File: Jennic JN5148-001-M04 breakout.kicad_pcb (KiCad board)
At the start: 2 copper layers, 45.7 x 55.9 mm, 23 parts, among them J1 Conn_01x21_Male, J2 Conn_01x21_Male, J9 Conn_01x06_Male, SW1 SW_Push, SW2 SW_Push, SW5 SW_Push, SW7 SW_Push, U1 JN5148-001-M04, U2 NCP1117LPST33T3G

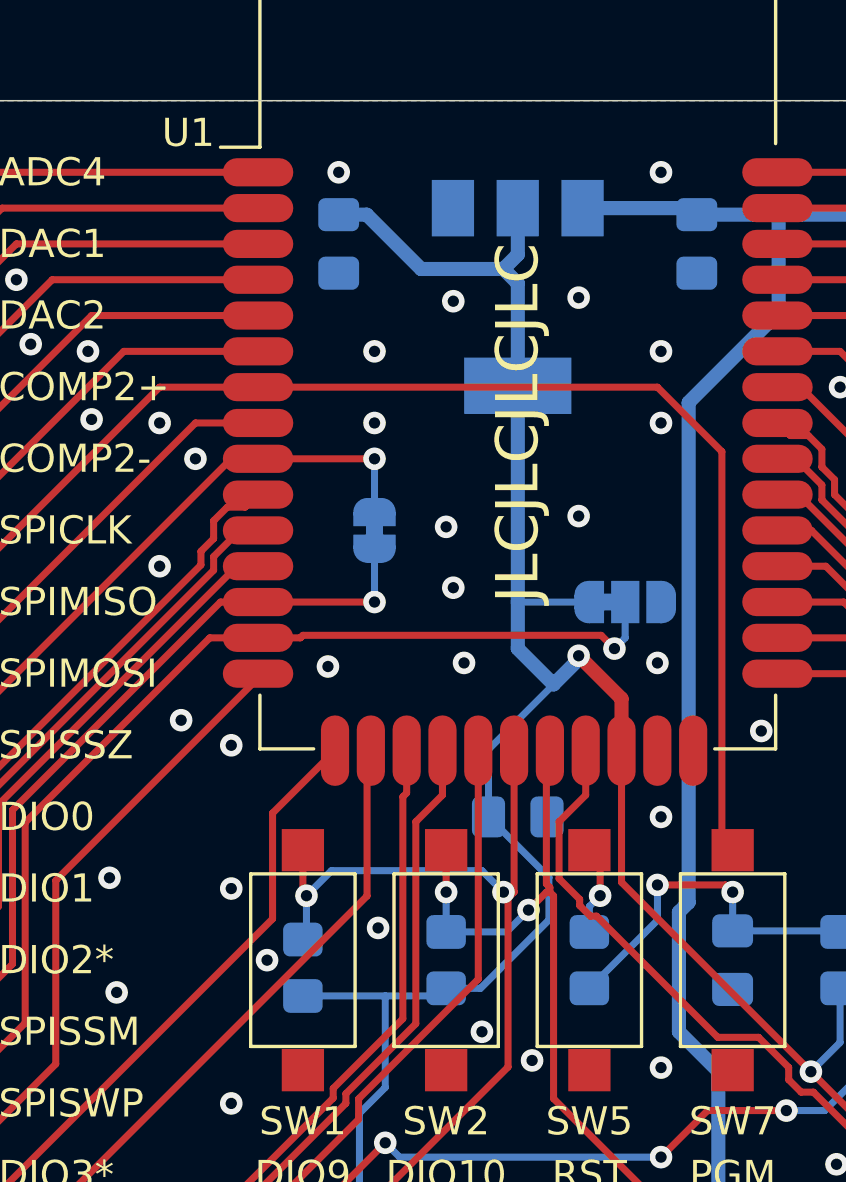
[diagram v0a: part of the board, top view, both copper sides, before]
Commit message: Aligned resistor R3.
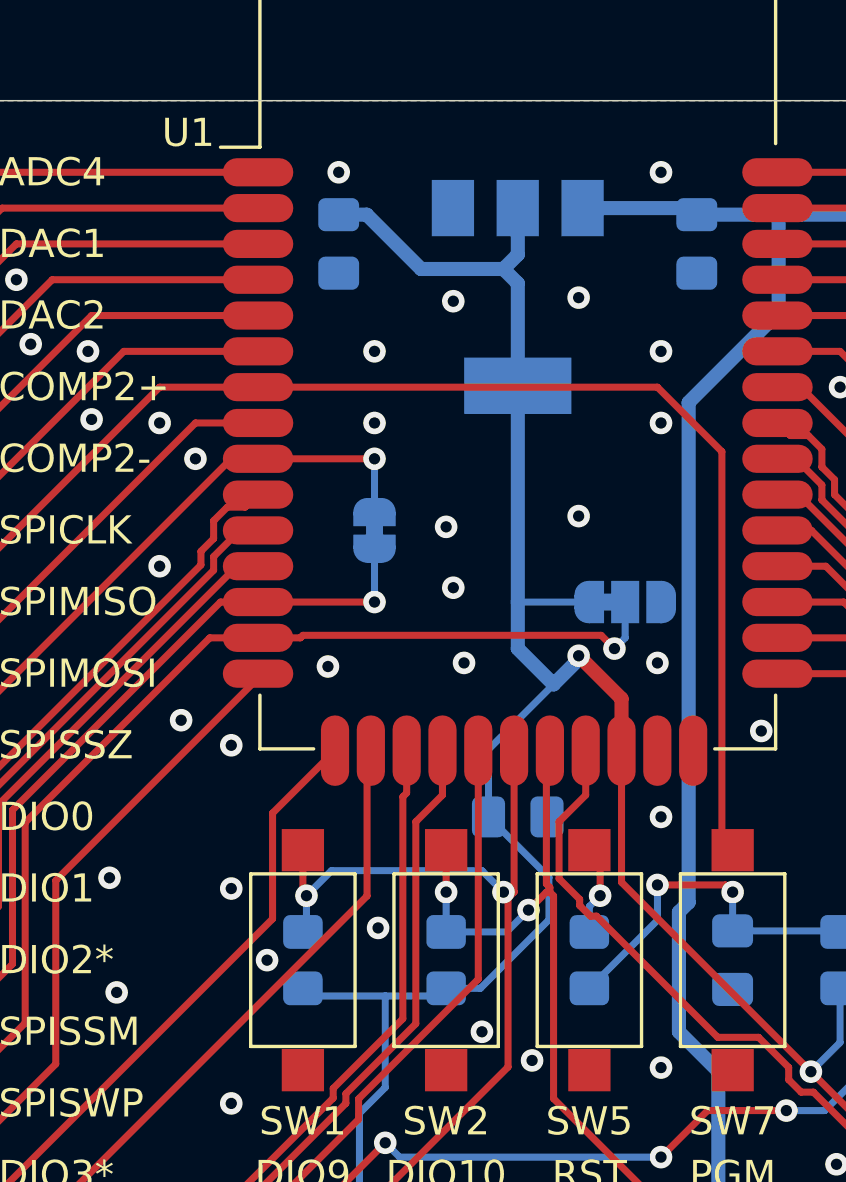
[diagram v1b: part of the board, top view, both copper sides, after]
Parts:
- moved R3 0.27 mm to (137.2, 104.1)
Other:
- board text added: "JN5148-001-M04 module breakout 2021-11-14 V1.1"
- board text removed: "JLCJLCJLCJLC"
- board text removed: "JN5148-001-M04 module breakout 2021-02-24 V1.0"
